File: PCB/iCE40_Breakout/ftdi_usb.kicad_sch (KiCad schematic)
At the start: 58 parts, among them J5 USB_C_Receptacle_USB2.0_16P, J6 Conn_01x08, Q13 L2N7002SLLT1G, Q14 L2N7002SLLT1G, Q15 L2N7002SLLT1G, Q16 L2N7002SLLT1G, U7 FT2232HPQ, U8 93LC66BT-I/SN, Y1 X3S012000FK1H-HV

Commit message: Changed all pin sockets to be headers
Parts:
- J6: footprint Connector_PinSocket_2.54mm:PinSocket_1x10_P2.54mm_Vertical -> Connector_PinHeader_2.54mm:PinHeader_1x10_P2.54mm_Vertical
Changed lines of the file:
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@@
 			)
 		)
-		(property "Footprint" "Connector_PinSocket_2.54mm:PinSocket_1x10_P2.54mm_Vertical"
+		(property "Footprint" "Connector_PinHeader_2.54mm:PinHeader_1x10_P2.54mm_Vertical"
 			(at 255.27 97.79 0)
 			(effects

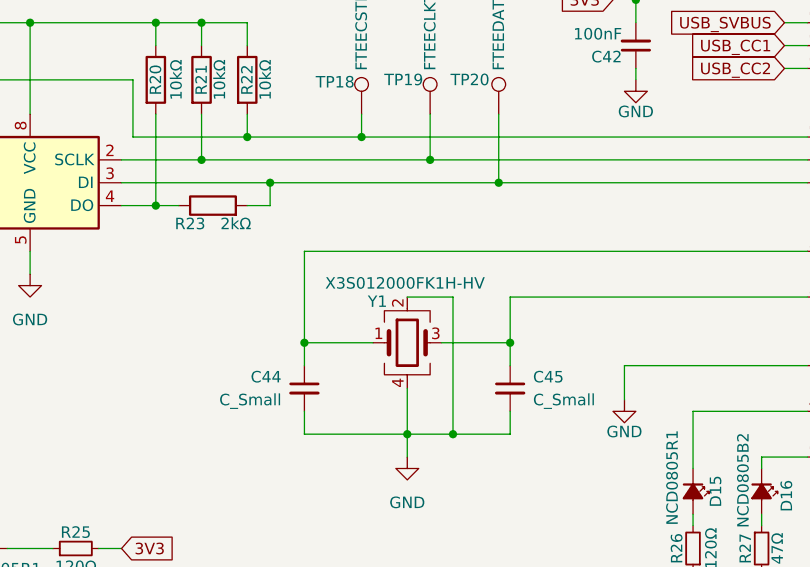
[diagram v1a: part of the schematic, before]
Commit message: Changed XTAL to be a JLCPCB basic part
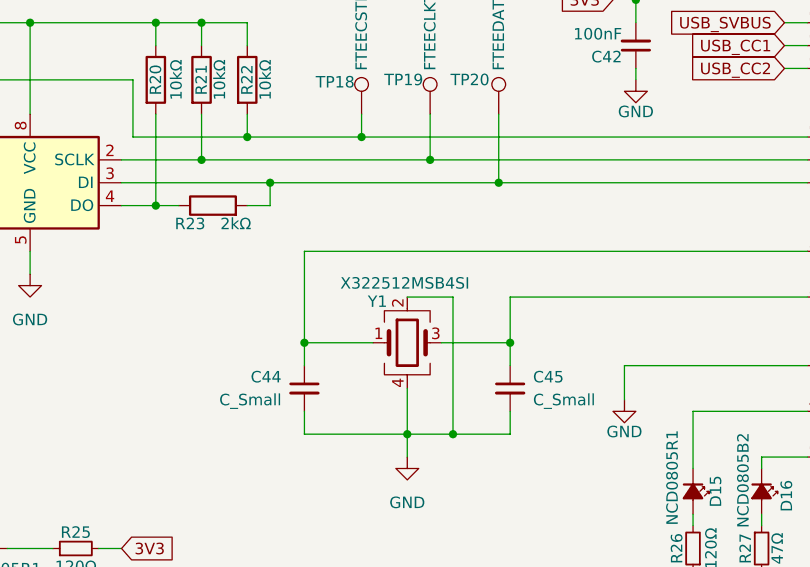
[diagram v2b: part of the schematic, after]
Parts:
- Y1: value X3S012000FK1H-HV -> X322512MSB4SI; LCSC C254309 -> C9002
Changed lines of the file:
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@@
 			)
 		)
-		(property "Value" "X3S012000FK1H-HV"
+		(property "Value" "X322512MSB4SI"
 			(at 134.366 124.206 0)
 			(effects
@@
 			)
 		)
-		(property "Datasheet" "kicad-embed://XTAL-X3S012000FK1H-HV.pdf"
+		(property "Datasheet" "kicad-embed://XTAL-YXC-X322512MSB4SI.pdf"
 			(at 134.62 130.81 0)
 			(effects
@@
 			)
 		)
-		(property "LCSC" " C254309"
+		(property "LCSC" "C9002"
 			(at 134.62 130.81 0)
 			(effects

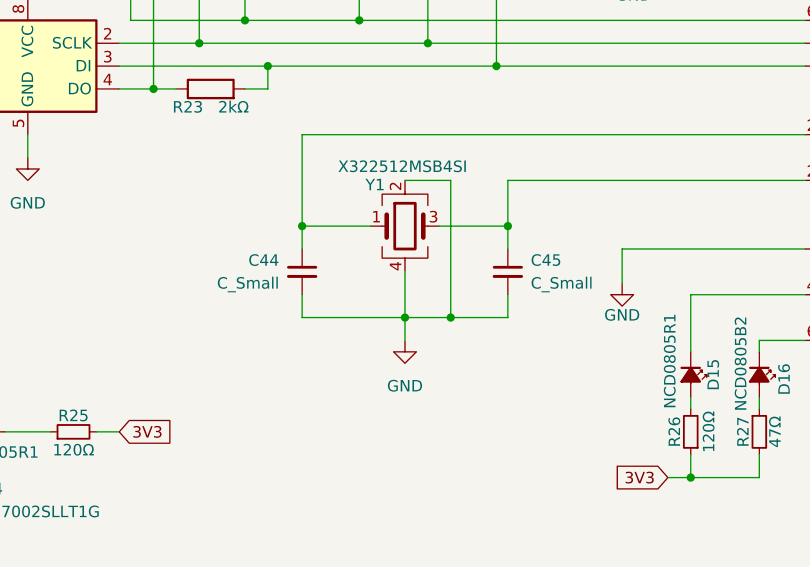
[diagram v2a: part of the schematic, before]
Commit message: Guessed XTAL caps at 15pF
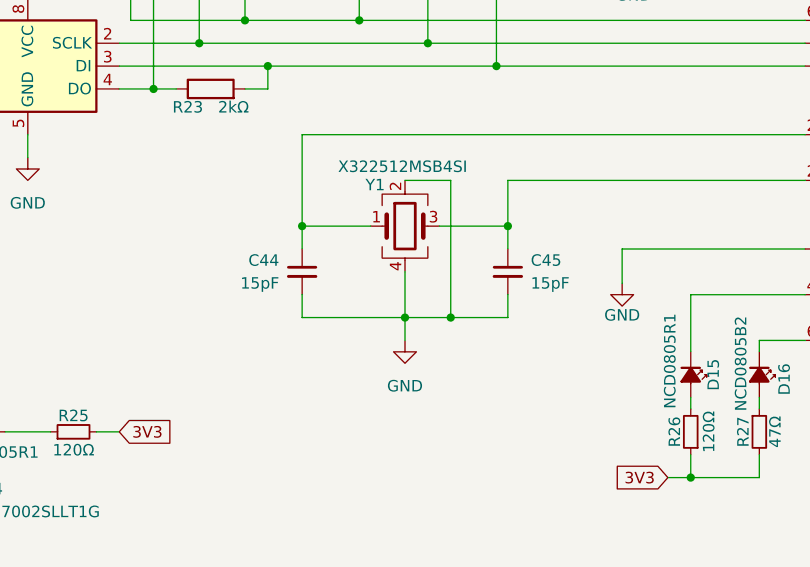
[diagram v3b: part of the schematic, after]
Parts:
- C44, C45: value C_Small -> 15pF; LCSC (none) -> C1548
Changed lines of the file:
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@@
+	)
+	(symbol
+		(lib_id "Interface_FTDI:FT2232HPQ")
+		(at 210.82 93.98 0)
+		(unit 1)
+		(exclude_from_sim no)
+		(in_bom yes)
+		(on_board yes)
+		(dnp no)
+		(property "Reference" "U7"
+			(at 210.82 92.964 0)
+			(effects
+				(font
+					(size 1.524 1.524)
+				)
+			)
+		)
+		(property "Value" "FT2232HPQ"
+			(at 210.82 95.504 0)
+			(effects
+				(font
+					(size 1.524 1.524)
+				)
+			)
+		)
+		(property "Footprint" "Interface_FTDI:QFN68_FT2232"
+			(at 210.82 17.272 0)
+			(effects
+				(font
+					(size 1.27 1.27)
+					(italic yes)
+				)
+				(hide yes)
+			)
+		)
+		(property "Datasheet" "kicad-embed://DS_FT2233HP.pdf"
+			(at 210.82 12.446 0)
+			(effects
+				(font
+					(size 1.27 1.27)
+					(italic yes)
+				)
+				(hide yes)
+			)
+		)
+		(property "Description" "FTDI dual channel USB interface chip with PD support"
+			(at 211.074 14.986 0)
+			(effects
+				(font
+					(size 1.27 1.27)
+				)
+				(hide yes)
+			)
+		)
+		(property "LCSC" "C3228146"
+			(at 210.82 93.98 0)
+			(effects
+				(font
+					(size 1.27 1.27)
+				)
+				(hide yes)
+			)
+		)
+		(pin "31"
+		)
+		(pin "63"
+		)
+		(pin "68"
+		)
+		(pin "2"
+		)
+		(pin "27"
+		)
+		(pin "28"
+		)
+		(pin "64"
+		)
+		(pin "58"
+		)
+		(pin "3"
+		)
+		(pin "43"
+		)
+		(pin "67"
+		)
+		(pin "30"
+		)
+		(pin "60"
+		)
+		(pin "33"
+		)
+		(pin "59"
+		)
+		(pin "4"
+		)
+		(pin "32"
+		)
+		(pin "65"
+		)
+		(pin "62"
+		)
+		(pin "1"
+		)
+		(pin "8"
+		)
+		(pin "66"
+		)
+		(pin "61"
+		)
+		(pin "29"
+		)
+		(pin "44"
+		)
+		(pin "39"
+		)
+		(pin "26"
+		)
+		(pin "51"
+		)
+		(pin "57"
+		)
+		(pin "9"
+		)
+		(pin "25"
+		)
+		(pin "69"
+		)
+		(pin "10"
+		)
+		(pin "34"
+		)
+		(pin "36"
+		)
+		(pin "23"
+		)
+		(pin "19"
+		)
+		(pin "13"
+		)
+		(pin "35"
+		)
+		(pin "11"
+		)
+		(pin "37"
+		)
+		(pin "38"
+		)
+		(pin "14"
+		)
+		(pin "12"
+		)
+		(pin "6"
+		)
+		(pin "7"
+		)
+		(pin "15"
+		)
+		(pin "16"
+		)
+		(pin "20"
+		)
+		(pin "22"
+		)
+		(pin "21"
+		)
+		(pin "18"
+		)
+		(pin "17"
+		)
+		(pin "24"
+		)
+		(pin "48"
+		)
+		(pin "42"
+		)
+		(pin "55"
+		)
+		(pin "50"
+		)
+		(pin "5"
+		)
+		(pin "53"
+		)
+		(pin "46"
+		)
+		(pin "56"
+		)
+		(pin "41"
+		)
+		(pin "40"
+		)
+		(pin "45"
+		)
+		(pin "52"
+		)
+		(pin "54"
+		)
+		(pin "47"
+		)
+		(pin "49"
+		)
+		(instances
+			(project "iCE40_Breakout"
+				(path "/ce4d7974-ef38-4eea-8119-381c4298ef02/a0447fef-6cc5-400b-aa41-8540b8ebce1f"
+					(reference "U7")
+					(unit 1)
+				)
+			)
+		)
 	)
 	(symbol
@@
 		(on_board yes)
 		(dnp no)
-		(fields_autoplaced yes)
 		(property "Reference" "C45"
 			(at 148.59 134.6262 0)
@@
 			)
 		)
-		(property "Value" "C_Small"
+		(property "Value" "15pF"
 			(at 148.59 137.1662 0)
 			(effects
@@
 			)
 		)
+		(property "LCSC" "C1548"
+			(at 146.05 135.89 0)
+			(effects
+				(font
+					(size 1.27 1.27)
+				)
+				(hide yes)
+			)
+		)
 		(pin "2"
 		)
@@
 				(path "/ce4d7974-ef38-4eea-8119-381c4298ef02/a0447fef-6cc5-400b-aa41-8540b8ebce1f"
 					(reference "C45")
-					(unit 1)
-				)
-			)
-		)
-	)
-	(symbol
-		(lib_id "Interface_FTDI:FT2232HPQ")
-		(at 210.82 93.98 0)
-		(unit 1)
-		(exclude_from_sim no)
-		(in_bom yes)
-		(on_board yes)
-		(dnp no)
-		(property "Reference" "U7"
-			(at 210.82 92.964 0)
-			(effects
-				(font
-					(size 1.524 1.524)
-				)
-			)
-		)
-		(property "Value" "FT2232HPQ"
-			(at 210.82 95.504 0)
-			(effects
-				(font
-					(size 1.524 1.524)
-				)
-			)
-		)
-		(property "Footprint" "Interface_FTDI:QFN68_FT2232"
-			(at 210.82 17.272 0)
-			(effects
-				(font
-					(size 1.27 1.27)
-					(italic yes)
-				)
-				(hide yes)
-			)
-		)
-		(property "Datasheet" "kicad-embed://DS_FT2233HP.pdf"
-			(at 210.82 12.446 0)
-			(effects
-				(font
-					(size 1.27 1.27)
-					(italic yes)
-				)
-				(hide yes)
-			)
-		)
-		(property "Description" "FTDI dual channel USB interface chip with PD support"
-			(at 211.074 14.986 0)
-			(effects
-				(font
-					(size 1.27 1.27)
-				)
-				(hide yes)
-			)
-		)
-		(property "LCSC" "C3228146"
-			(at 210.82 93.98 0)
-			(effects
-				(font
-					(size 1.27 1.27)
-				)
-				(hide yes)
-			)
-		)
-		(pin "31"
-		)
-		(pin "63"
-		)
-		(pin "68"
-		)
-		(pin "2"
-		)
-		(pin "27"
-		)
-		(pin "28"
-		)
-		(pin "64"
-		)
-		(pin "58"
-		)
-		(pin "3"
-		)
-		(pin "43"
-		)
-		(pin "67"
-		)
-		(pin "30"
-		)
-		(pin "60"
-		)
-		(pin "33"
-		)
-		(pin "59"
-		)
-		(pin "4"
-		)
-		(pin "32"
-		)
-		(pin "65"
-		)
-		(pin "62"
-		)
-		(pin "1"
-		)
-		(pin "8"
-		)
-		(pin "66"
-		)
-		(pin "61"
-		)
-		(pin "29"
-		)
-		(pin "44"
-		)
-		(pin "39"
-		)
-		(pin "26"
-		)
-		(pin "51"
-		)
-		(pin "57"
-		)
-		(pin "9"
-		)
-		(pin "25"
-		)
-		(pin "69"
-		)
-		(pin "10"
-		)
-		(pin "34"
-		)
-		(pin "36"
-		)
-		(pin "23"
-		)
-		(pin "19"
-		)
-		(pin "13"
-		)
-		(pin "35"
-		)
-		(pin "11"
-		)
-		(pin "37"
-		)
-		(pin "38"
-		)
-		(pin "14"
-		)
-		(pin "12"
-		)
-		(pin "6"
-		)
-		(pin "7"
-		)
-		(pin "15"
-		)
-		(pin "16"
-		)
-		(pin "20"
-		)
-		(pin "22"
-		)
-		(pin "21"
-		)
-		(pin "18"
-		)
-		(pin "17"
-		)
-		(pin "24"
-		)
-		(pin "48"
-		)
-		(pin "42"
-		)
-		(pin "55"
-		)
-		(pin "50"
-		)
-		(pin "5"
-		)
-		(pin "53"
-		)
-		(pin "46"
-		)
-		(pin "56"
-		)
-		(pin "41"
-		)
-		(pin "40"
-		)
-		(pin "45"
-		)
-		(pin "52"
-		)
-		(pin "54"
-		)
-		(pin "47"
-		)
-		(pin "49"
-		)
-		(instances
-			(project "iCE40_Breakout"
-				(path "/ce4d7974-ef38-4eea-8119-381c4298ef02/a0447fef-6cc5-400b-aa41-8540b8ebce1f"
-					(reference "U7")
 					(unit 1)
 				)
@@
 			)
 		)
-		(property "Value" "C_Small"
+		(property "Value" "15pF"
 			(at 120.65 137.1662 0)
 			(effects
@@
 			(at 123.19 135.89 0)
 			(effects
+				(font
+					(size 1.27 1.27)
+				)
+				(hide yes)
+			)
+		)
+		(property "LCSC" "C1548"
+			(at 123.19 135.89 0)
+			(effects
